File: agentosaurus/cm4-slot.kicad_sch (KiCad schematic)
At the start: 1 part, among them T1 HX1188NL

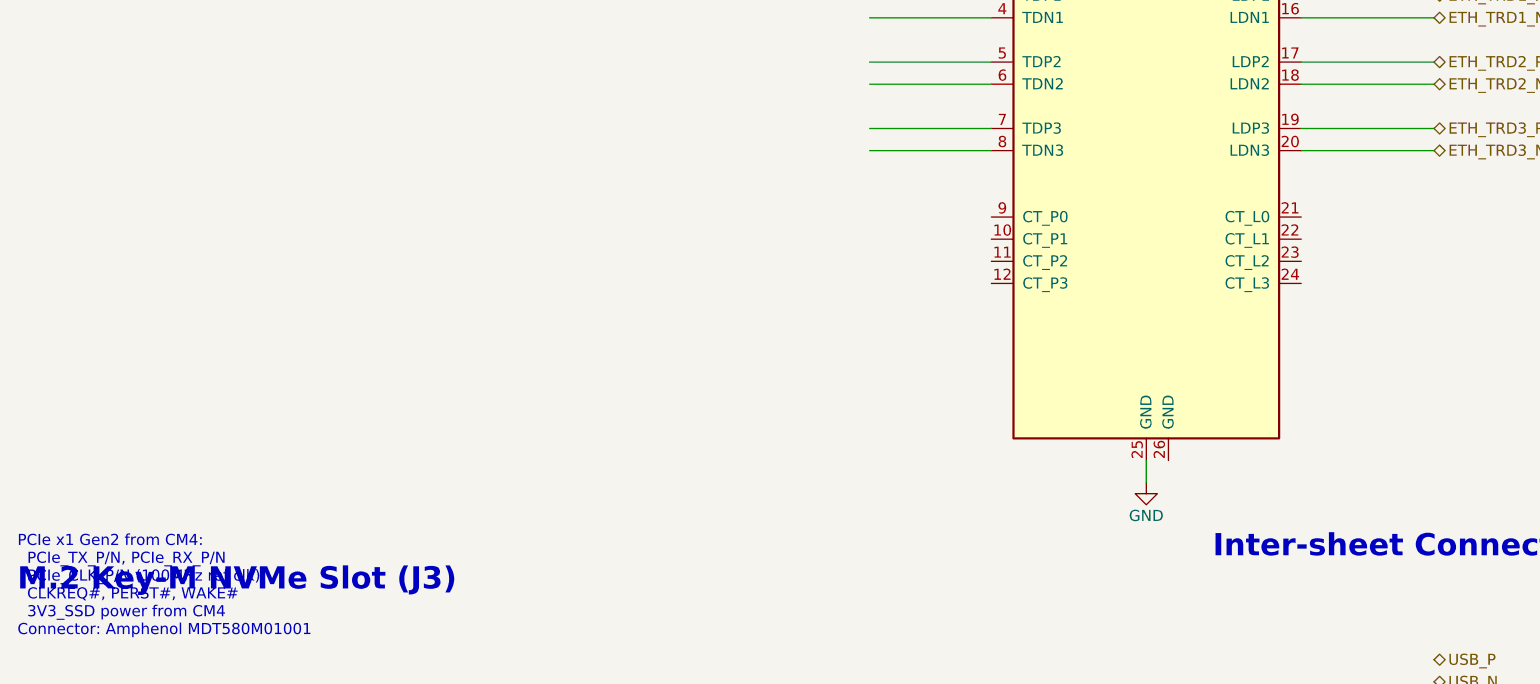
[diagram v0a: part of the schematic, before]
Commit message: Add passive components to all schematic sheets
- power.kicad_sch: Fix D1 catch diode rotation (cathode→SW), remove
  incorrect COMP-to-output wire, add all TPS54360 application circuit
  passives (CIN1/2, CBOOT, L1, COUT1-3, R_EN1/2, R_RT, R_FB1/2,
  R_COMP, C_COMP) and AMS1117 caps (CIN_LDO, COUT_LDO)
- bmc.kicad_sch: Add USB-C CC pull-downs (R1/R2 5.1k), ESP32 reset
  circuit (R3 10k + C9 1uF), decoupling caps for ESP32 (C10/C11),
  UART mux (C12), USB mux (C13/C14), WS2812B (C15-C18), I2C
  pull-ups (R4/R5 4.7k)
- cm4-slot.kicad_sch: Add magnetics center-tap decoupling (C1-C4
  100nF) and power rail decoupling (C5-C8)
- ethernet-switch.kicad_sch: Add crystal load caps (C1/C2 22pF),
  3.3V decoupling (C3-C10), 1.0V core decoupling (C11-C16),
  Slot 2 Ethernet wiring to RTL8367S
- mechanical.kicad_sch: Add PCB stackup, impedance control, and
  via specifications

https://claude.ai/code/session_01UhhXLgEHsAy83XEALyNrDb
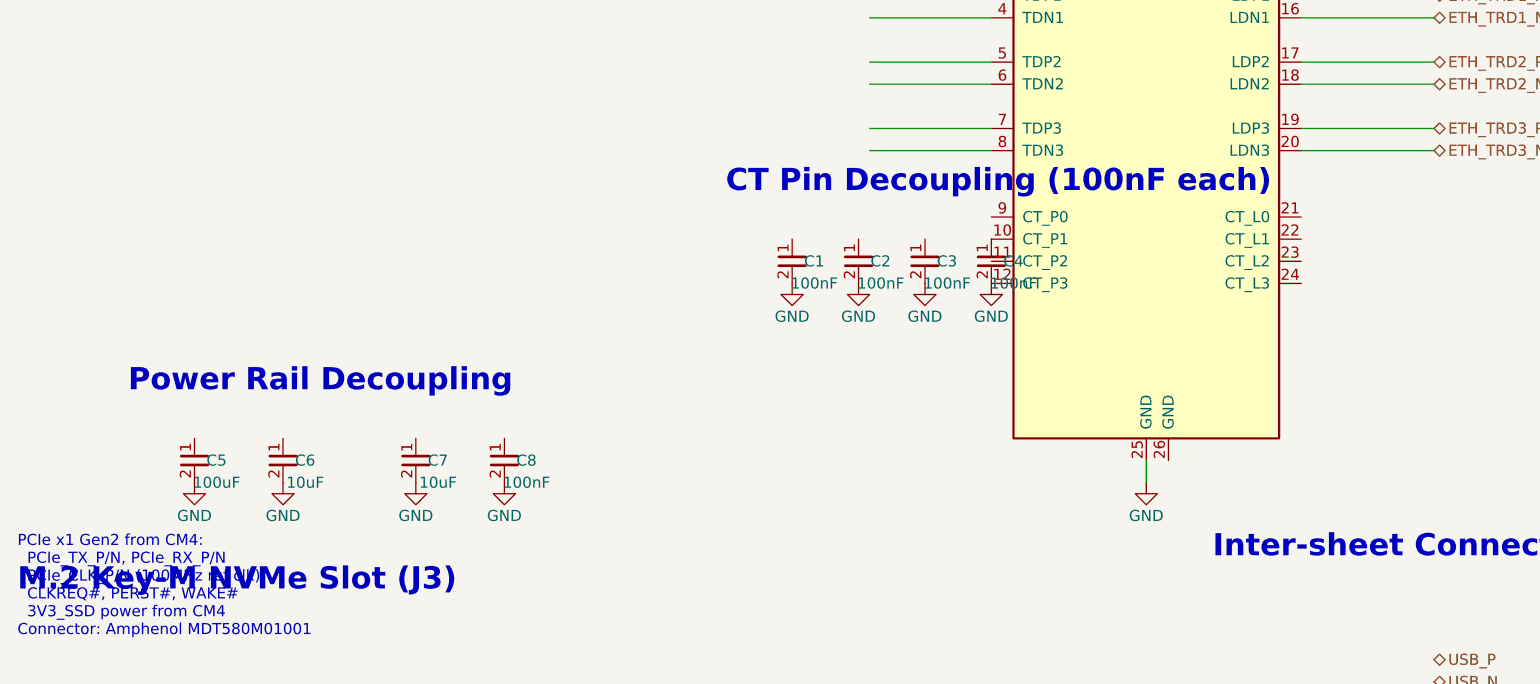
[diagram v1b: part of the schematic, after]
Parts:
- added C1, C2, C3, C4, C8: 100nF, Capacitor_SMD:C_0402_1005Metric, symbol Device:C
- added C5: 100uF, Capacitor_SMD:C_1210_3225Metric, symbol Device:C
- added C6, C7: 10uF, Capacitor_SMD:C_0805_2012Metric, symbol Device:C
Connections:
- net GND: now also T1.12 (CT_P3), C1.2, C2.2, C3.2, C4.2, C5.2, C6.2, C7.2, C8.2
- net at T1.10 (CT_P1): now also C4.1
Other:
- note added: "CT Pin Decoupling (100nF each)"
- note added: "Power Rail Decoupling"

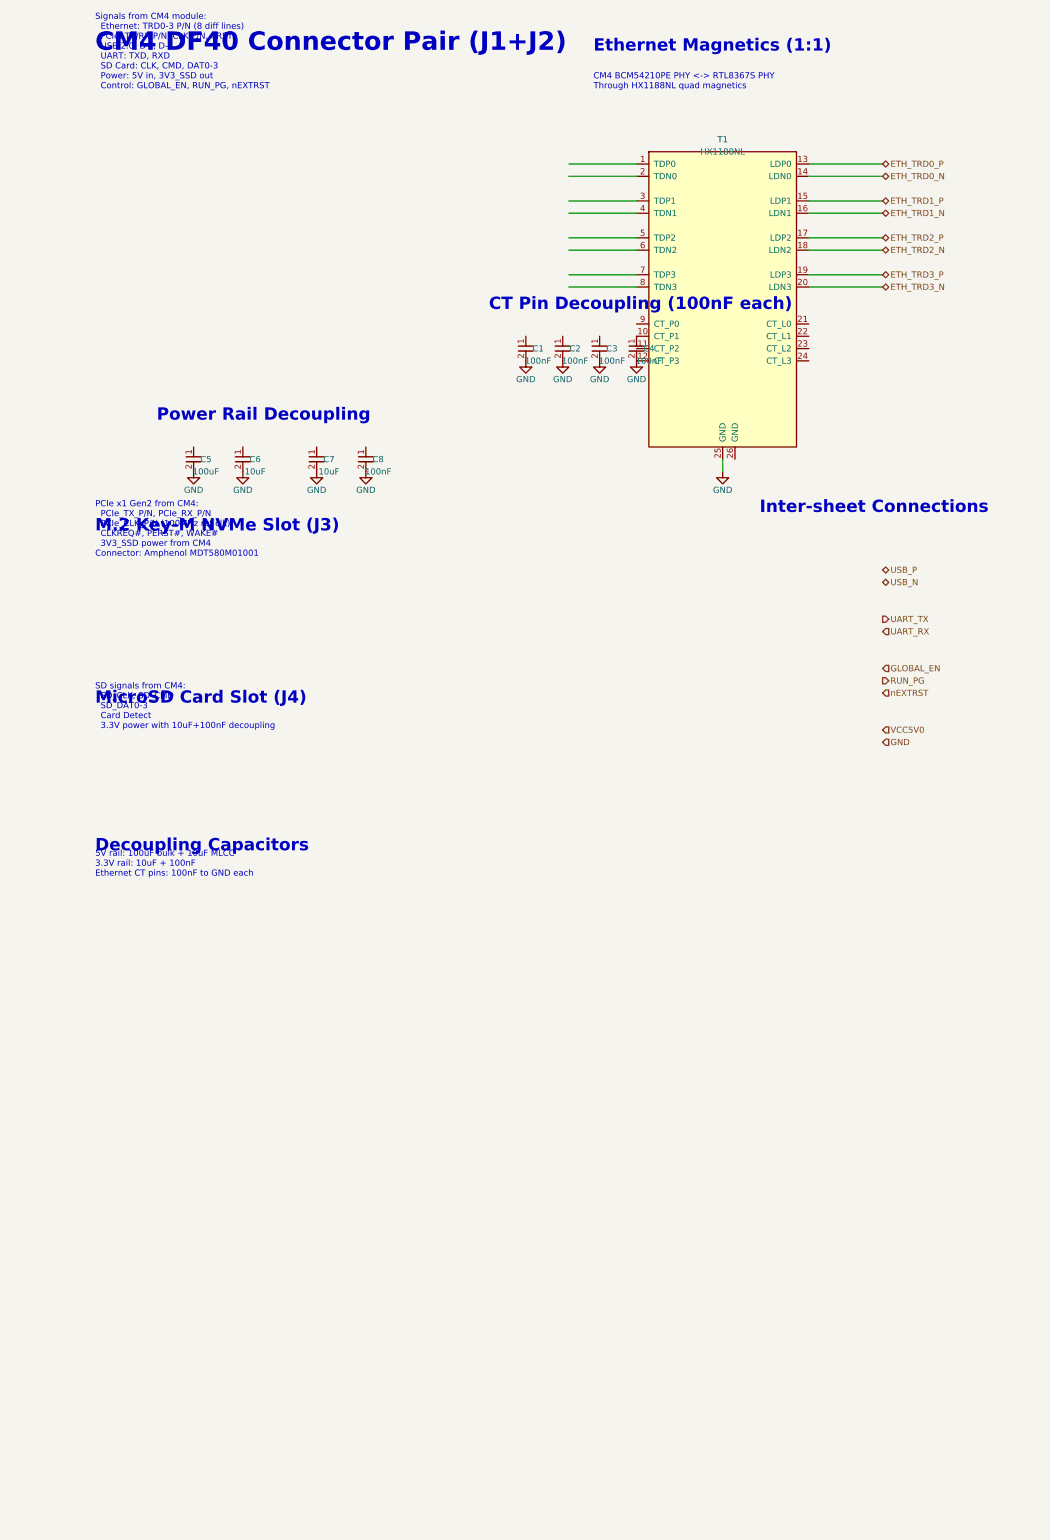
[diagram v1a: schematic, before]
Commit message: Add DF40, M.2 NVMe, and microSD connectors to CM4 slot
- J1+J2: DF40HC-100DS connector pair with CM4 pin assignments
  (Ethernet TRD0-3, USB, UART, PCIe, SD, control, power)
- J3: M.2 Key-M NVMe slot with PCIe x1 lane, ref clock, PERST#
- J4: MicroSD card slot with SDIO signals and card detect
- Net labels connecting DF40 pins to existing magnetics and
  hierarchical labels (USB, UART, control, power)
- Power symbols for VCC5V0, VCC3V3, VCC3V3_SSD rails

https://claude.ai/code/session_01UhhXLgEHsAy83XEALyNrDb
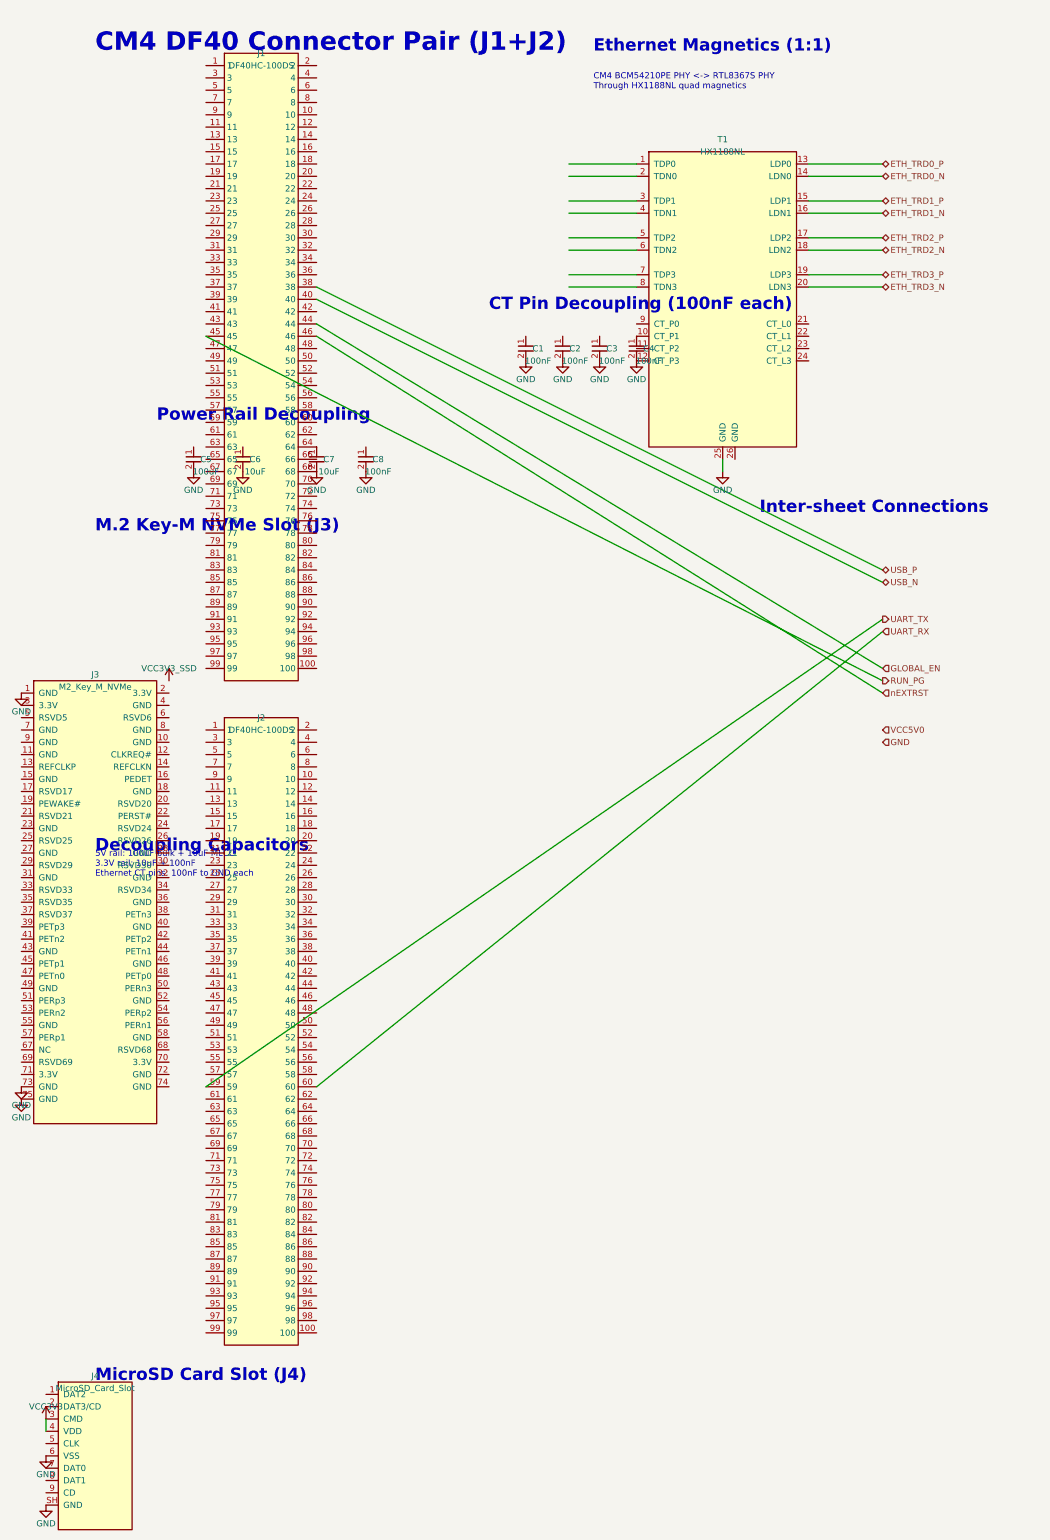
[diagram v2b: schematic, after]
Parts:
- added J1, J2: DF40HC-100DS, scalenode-cm4-baseboard-footprints:DF40HC(3.0)-100DS-0.4v, symbol scalenode-cm4-baseboard:DF40HC(3.0)-100DS-0.4v
- added J3: M2_Key_M_NVMe, agentosaurus-footprints:M2_Key_M_2280, symbol agentosaurus:M2_Key_M_NVMe
- added J4: MicroSD_Card_Slot, agentosaurus-footprints:MicroSD_Card_Slot, symbol agentosaurus:MicroSD_Card_Slot
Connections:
- net GLOBAL_EN: now also J1.44
- net GND: now also J1.68, J3.1 (GND), J3.73 (GND), J3.75 (GND), J4.6 (VSS), J4.SH (GND)
- net RUN_PG: now also J1.45
- net UART_RX: now also J2.60
- net UART_TX: now also J2.59
- net USB_N: now also J1.40
- net USB_P: now also J1.38
- net nEXTRST: now also J1.46
- net at C7.1: now also J1.64
- new net VCC3V3: J4.3 (CMD), J4.4 (VDD)
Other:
- note removed: "PCIe x1 Gen2 from CM4: PCIe_TX_P/N, PCIe_RX_P/N PCIe_CLK_P/N (100MHz ref clk) CLKREQ#, PERST#, WAKE# 3V3_SSD power from CM4 Connector: Amphenol MDT580M01001"
- note removed: "SD signals from CM4: SD_CLK, SD_CMD SD_DAT0-3 Card Detect 3.3V power with 10uF+100nF decoupling"
- note removed: "Signals from CM4 module: Ethernet: TRD0-3 P/N (8 diff lines) PCIe: TX/RX P/N, CLK P/N, nRST USB 2.0: D+, D- UART: TXD, RXD SD Card: CLK, CMD, DAT0-3 Power: 5V in, 3V3_SSD out Control: GLOBAL_EN, RUN_PG, nEXTRST"
